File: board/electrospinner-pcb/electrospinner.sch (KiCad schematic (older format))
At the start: 38 parts, among them J1 Header_02x02, SW1 ResetBTN, U1 FT230XS, U2 TPS62147, U3 TPS62147, U5 MSP430G2553IPW20

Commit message: Finishes rev2 of schematic
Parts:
- removed C1: 10uF, Capacitor_SMD:C_0805_2012Metric, symbol electrospinner-rescue:C_Small-Device-electrospinner-rescue
- removed C3: 3.3uF, Capacitor_SMD:C_0805_2012Metric, symbol Device:C_Small
- removed C5: 2.2uF, Capacitor_SMD:C_0805_2012Metric, symbol electrospinner-rescue:C_Small-Device-electrospinner-rescue
- removed C? (x3): 0.1uF, symbol Device:C_Small
- removed C?: 100uF, symbol Device:CP1_Small
- removed L1: 1uH, Inductor_SMD:L_0805_2012Metric, symbol electrospinner-rescue:L_Small-Device-electrospinner-rescue
- removed R1: 470k, Resistor_SMD:R_0805_2012Metric, symbol electrospinner-rescue:R_Small_US-Device-electrospinner-rescue
- removed R2: 100k, Resistor_SMD:R_0805_2012Metric, symbol electrospinner-rescue:R_Small_US-Device-electrospinner-rescue
- removed R8: 158, Resistor_SMD:R_0805_2012Metric, symbol Device:R_US
- removed U2: TPS62147, footprints:TPS62147RGXR, symbol electrospinner-rescue:TPS62147-Regulator_Switching-electrospinner-rescue-electr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
- added C1: 0.1uF, Capacitor_SMD:C_0805_2012Metric, symbol Device:C_Small
- added C3: 100uF, Capacitor_SMD:CP_Elec_6.3x5.8, symbol Device:CP1_Small
- added C5, C7, C8, C9: 0.1uF, Capacitor_SMD:C_0603_1608Metric, symbol Device:C_Small
- added R1: 158, Resistor_SMD:R_0603, symbol Device:R_Small_US
- added R2: 100, Resistor_SMD:R_0805_2012Metric, symbol Device:R_Small_US
- A1: renamed from A?; value Pololu_Breakout_A4988-Driver_Motor -> A4988_Breakout; MPN (none) -> 2128; Manufacturer (none) -> Pololu
- C10: renamed from C?; value C_Small -> 0.1uF; footprint (none) -> Capacitor_SMD:C_0603_1608Metric; symbol Device:C_Small -> electrospinner-rescue:C_Small-Device; MPN (none) -> CGB1T3X6S0G104M022BB; Manufacturer (none) -> TDK
- C4: symbol Device:C_Small -> electrospinner-rescue:C_Small-Device
- D1, D2: symbol Device:LED_Small -> electrospinner-rescue:LED_Small-Device
- J1: symbol Connector_Generic:Conn_02x02_Counter_Clockwise -> electrospinner-rescue:Conn_02x02_Counter_Clockwise-Connector_Generic; Status (none) -> resource-center
- MotorConnector_Female1: symbol Connector:Conn_01x06_Female -> electrospinner-rescue:Conn_01x06_Female-Connector
- MotorConnector_Male1: symbol Connector:Conn_01x06_Male -> electrospinner-rescue:Conn_01x06_Male-Connector
- Pt1, U1, U5: Status ordered -> (none)
- R5, R6: symbol Device:R_Small_US -> electrospinner-rescue:R_Small_US-Device
- R7: value 1k -> 10k; symbol Device:R_Small_US -> electrospinner-rescue:R_Small_US-Device
- SW1: symbol Switch:SW_Push -> electrospinner-rescue:SW_Push-Switch
- StepperMotor1: symbol Motor:Stepper_Motor_unipolar_6pin -> electrospinner-rescue:Stepper_Motor_unipolar_6pin-Motor; MPN (none) -> 1200; Manufacturer (none) -> Pololu; Status ordered -> (none)
- Temp_Female1: symbol Connector:Conn_01x02_Female -> electrospinner-rescue:Conn_01x02_Female-Connector
- Temp_Male1: symbol Connector:Conn_01x02_Male -> electrospinner-rescue:Conn_01x02_Male-Connector
- U3: Status oredered -> (none)
- USB_B_Header1: symbol Connector:USB_B -> electrospinner-rescue:USB_B-Connector
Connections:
- net labels removed: +4V, +5V, ~MotorLABEL
- wire segments 183 -> 166
- no-connect marks 8 -> 12
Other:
- moved on the sheet: A1, Barrel_Jack1, C10, C2, C4, C6, J1, L2, MotorConnector_Female1, MotorConnector_Male1, R3, R4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

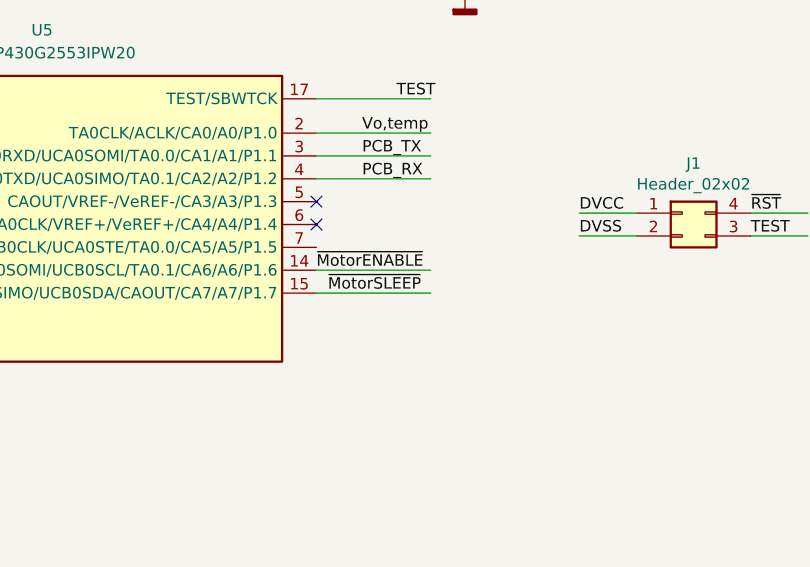
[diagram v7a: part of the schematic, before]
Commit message: Fixes typo: ~MotorRESET
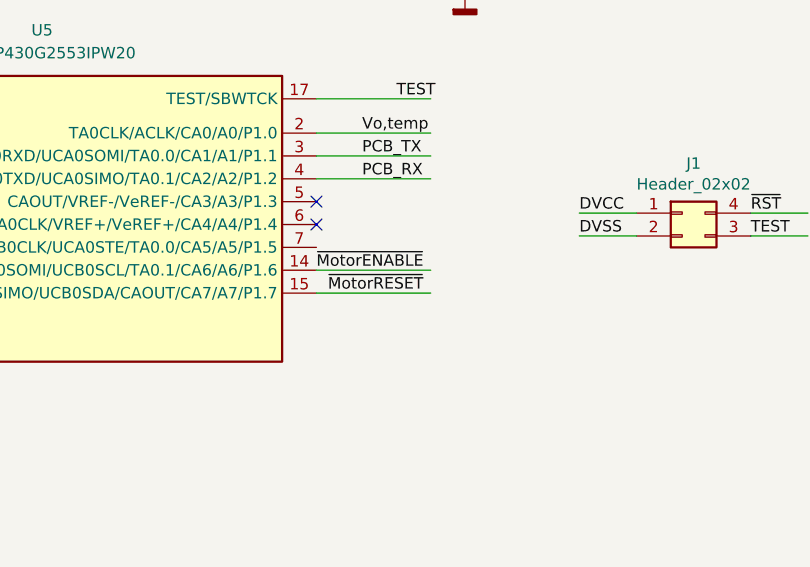
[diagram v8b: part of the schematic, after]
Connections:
- net labels added: ~MotorRESET
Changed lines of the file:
@@
 EESchema Schematic File Version 4
 LIBS:electrospinner-cache
-EELAYER 26 0
+EELAYER 29 0
 EELAYER END
 $Descr A4 11693 8268
@@
 ~MotorENABLE
 Text Label 8450 2750 0    50   ~ 0
-~MotorSLEEP
+~MotorRESET
 Wire Wire Line
 	8400 2750 8900 2750
